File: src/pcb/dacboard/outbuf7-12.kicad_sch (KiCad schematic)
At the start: 18 parts, among them U65 AD8675ARZ, U66 AD8675ARZ, U67 AD8675ARZ, U68 AD8675ARZ, U69 AD8675ARZ, U70 AD8675ARZ

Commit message: dacboard routing
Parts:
- C53, C54, C55, C56, C57, C58: footprint (none) -> Capacitor_SMD:C_0603_1608Metric_Pad1.08x0.95mm_HandSolder
- R22, R23, R24, R25, R26, R27: footprint (none) -> Resistor_SMD:R_0805_2012Metric
- U65, U66, U67, U68, U69, U70: footprint R_8_ADI -> Package_SO:SOIC-8_3.9x4.9mm_P1.27mm
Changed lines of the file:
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@@
 			)
 		)
-		(property "Footprint" ""
+		(property "Footprint" "Resistor_SMD:R_0805_2012Metric"
 			(at 263.144 52.324 90)
 			(effects
@@
 			)
 		)
-		(property "Footprint" ""
+		(property "Footprint" "Capacitor_SMD:C_0603_1608Metric_Pad1.08x0.95mm_HandSolder"
 			(at 40.3352 58.42 0)
 			(effects
@@
 			)
 		)
-		(property "Footprint" ""
+		(property "Footprint" "Capacitor_SMD:C_0603_1608Metric_Pad1.08x0.95mm_HandSolder"
 			(at 40.3352 137.16 0)
 			(effects
@@
 			)
 		)
-		(property "Footprint" "R_8_ADI"
+		(property "Footprint" "Package_SO:SOIC-8_3.9x4.9mm_P1.27mm"
 			(at 187.96 85.09 0)
 			(effects
@@
 			)
 		)
-		(property "Footprint" "R_8_ADI"
+		(property "Footprint" "Package_SO:SOIC-8_3.9x4.9mm_P1.27mm"
 			(at 57.15 127 0)
 			(effects
@@
 			)
 		)
-		(property "Footprint" ""
+		(property "Footprint" "Resistor_SMD:R_0805_2012Metric"
 			(at 132.334 131.064 90)
 			(effects
@@
 			)
 		)
-		(property "Footprint" ""
+		(property "Footprint" "Resistor_SMD:R_0805_2012Metric"
 			(at 263.144 128.524 90)
 			(effects
@@
 			)
 		)
-		(property "Footprint" ""
+		(property "Footprint" "Resistor_SMD:R_0805_2012Metric"
 			(at 132.334 52.324 90)
 			(effects
@@
 			)
 		)
-		(property "Footprint" ""
+		(property "Footprint" "Resistor_SMD:R_0805_2012Metric"
 			(at 263.144 89.154 90)
 			(effects
@@
 			)
 		)
-		(property "Footprint" ""
+		(property "Footprint" "Capacitor_SMD:C_0603_1608Metric_Pad1.08x0.95mm_HandSolder"
 			(at 171.1452 58.42 0)
 			(effects
@@
 			)
 		)
-		(property "Footprint" "R_8_ADI"
+		(property "Footprint" "Package_SO:SOIC-8_3.9x4.9mm_P1.27mm"
 			(at 57.15 48.26 0)
 			(effects
@@
 			)
 		)
-		(property "Footprint" ""
+		(property "Footprint" "Capacitor_SMD:C_0603_1608Metric_Pad1.08x0.95mm_HandSolder"
 			(at 171.1452 134.62 0)
 			(effects
@@
 			)
 		)
-		(property "Footprint" "R_8_ADI"
+		(property "Footprint" "Package_SO:SOIC-8_3.9x4.9mm_P1.27mm"
 			(at 57.15 85.09 0)
 			(effects
@@
 			)
 		)
-		(property "Footprint" ""
+		(property "Footprint" "Capacitor_SMD:C_0603_1608Metric_Pad1.08x0.95mm_HandSolder"
 			(at 40.3352 95.25 0)
 			(effects
@@
 			)
 		)
-		(property "Footprint" "R_8_ADI"
+		(property "Footprint" "Package_SO:SOIC-8_3.9x4.9mm_P1.27mm"
 			(at 187.96 124.46 0)
 			(effects
@@
 			)
 		)
-		(property "Footprint" "R_8_ADI"
+		(property "Footprint" "Package_SO:SOIC-8_3.9x4.9mm_P1.27mm"
 			(at 187.96 48.26 0)
 			(effects
@@
 			)
 		)
-		(property "Footprint" ""
+		(property "Footprint" "Capacitor_SMD:C_0603_1608Metric_Pad1.08x0.95mm_HandSolder"
 			(at 171.1452 95.25 0)
 			(effects
@@
 			)
 		)
-		(property "Footprint" ""
+		(property "Footprint" "Resistor_SMD:R_0805_2012Metric"
 			(at 132.334 89.154 90)
 			(effects

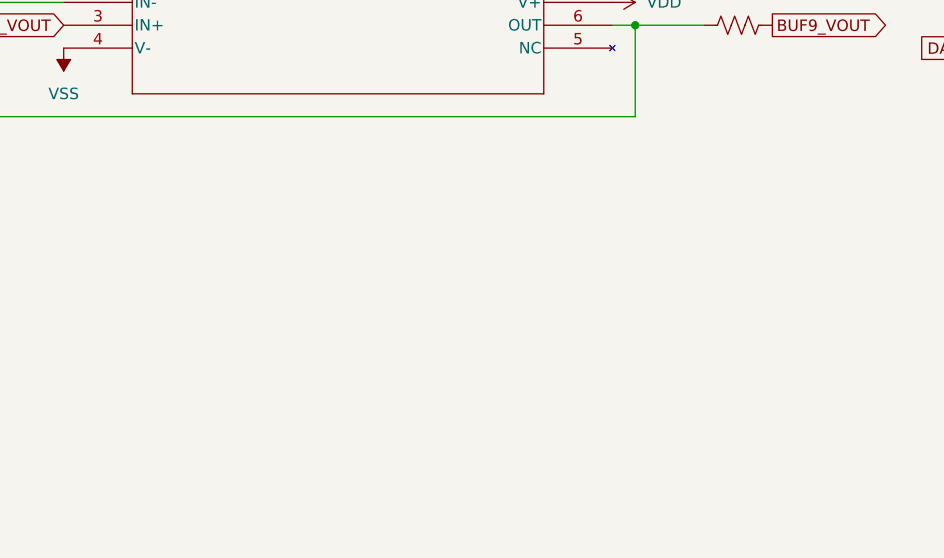
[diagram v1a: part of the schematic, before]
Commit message: got rid of all drc errors
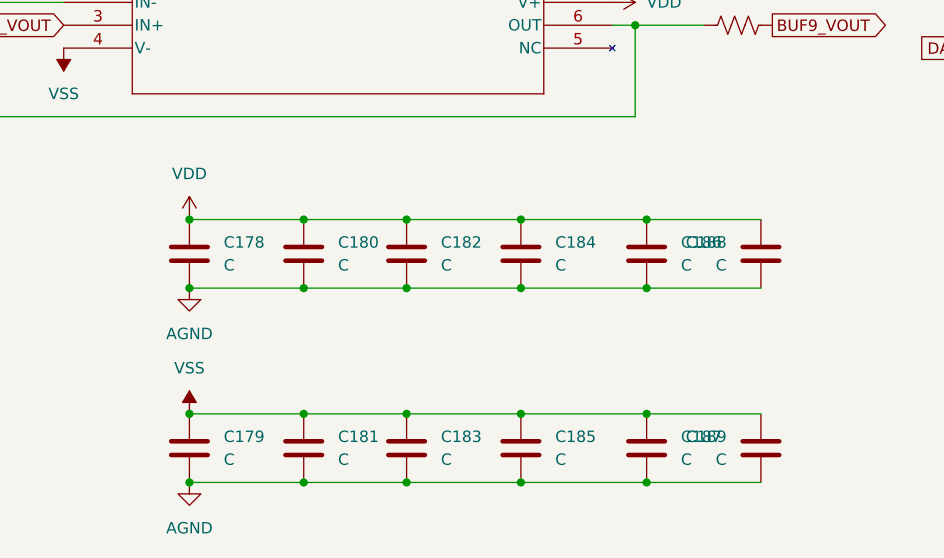
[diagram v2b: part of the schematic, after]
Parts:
- added C178, C179, C180, C181, C182, C183, C184, C185, C186, C187, C188, C189: C, Capacitor_SMD:C_0402_1005Metric_Pad0.74x0.62mm_HandSolder, symbol Device:C
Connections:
- net VDD: now also C178.1, C180.1, C182.1, C184.1, C186.1, C188.1
- net VSS: now also C179.1, C181.1, C183.1, C185.1, C187.1, C189.1
- new net AGND: C178.2, C179.2, C180.2, C181.2, C182.2, C183.2, C184.2, C185.2, C186.2, C187.2, C188.2, C189.2
